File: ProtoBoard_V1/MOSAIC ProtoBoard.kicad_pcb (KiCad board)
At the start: 2 copper layers, 89.5 x 90 mm, 10 parts, among them J7 Qwiic Adapter, J8 Qwiic Adapter, J9 Qwiic Adapter

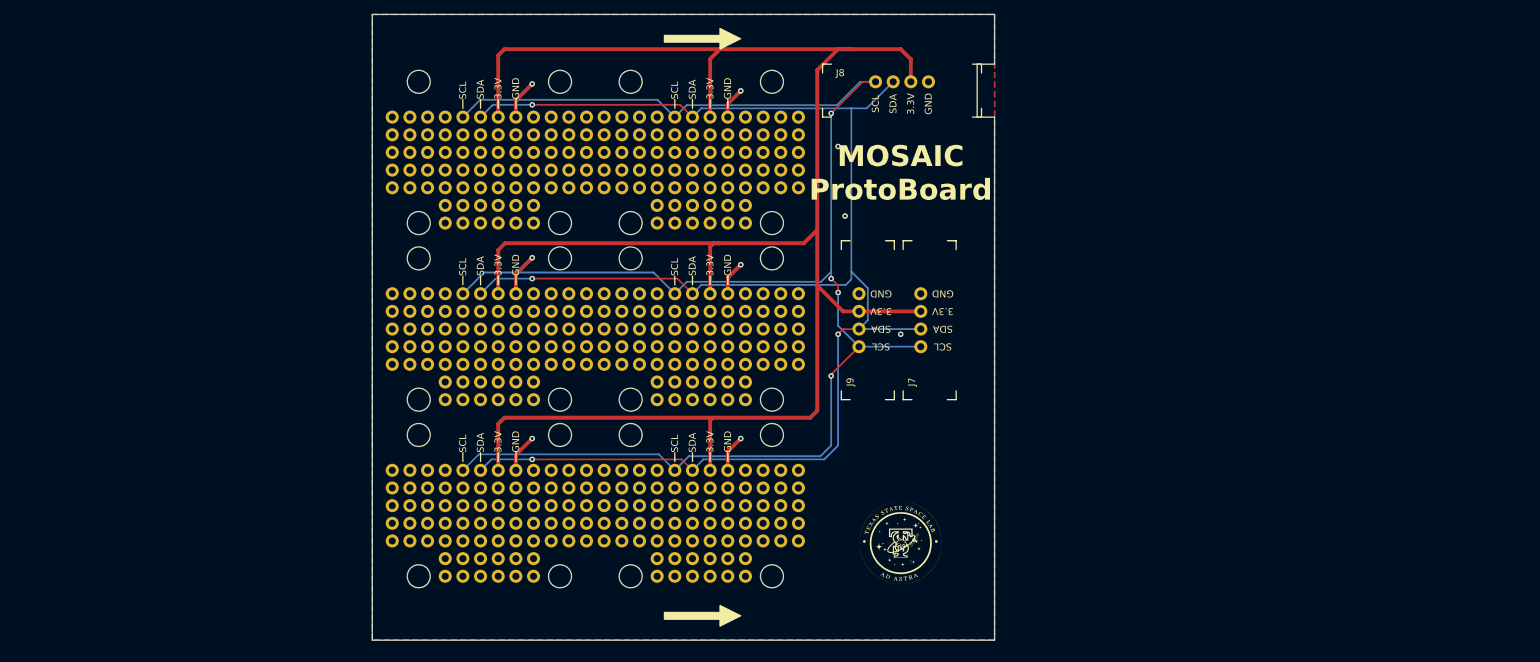
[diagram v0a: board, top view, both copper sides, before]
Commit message: Created new edge cut
Created new edge cut for the board based on new standard size
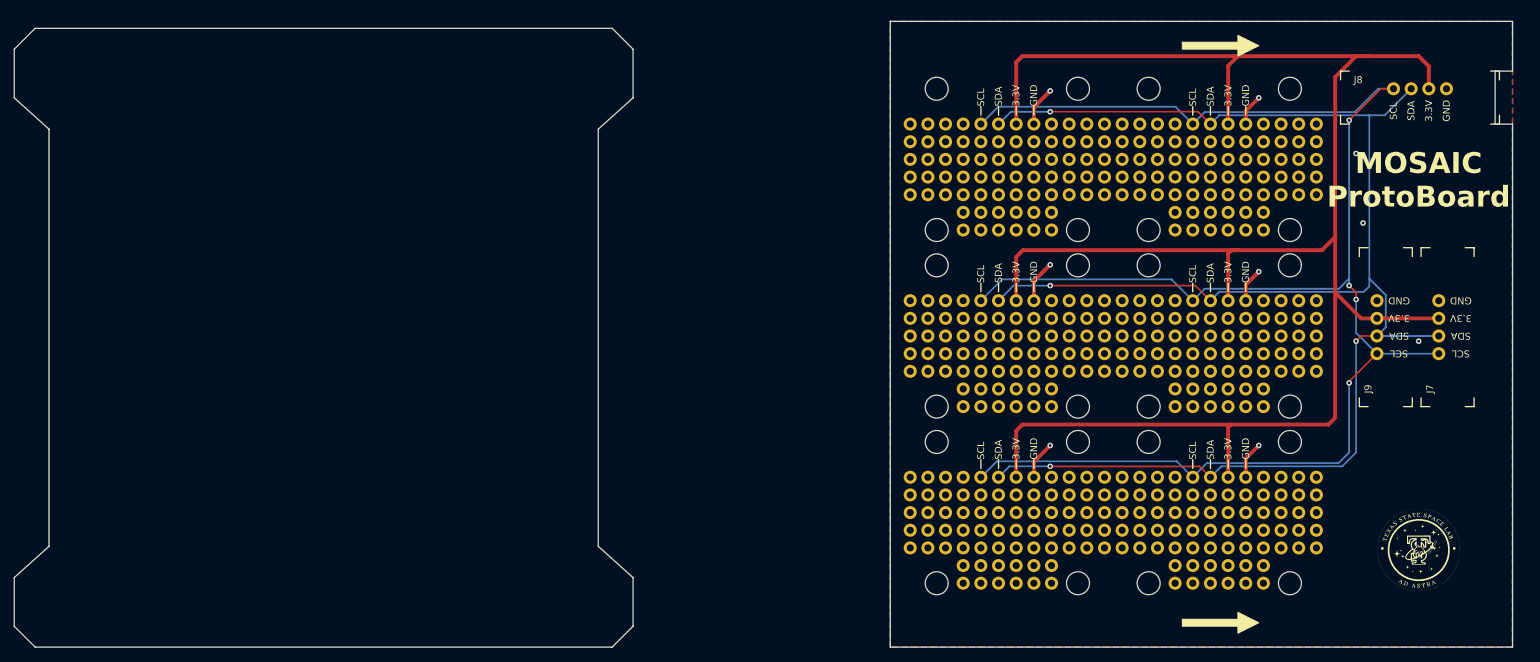
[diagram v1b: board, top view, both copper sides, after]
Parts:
- moved G*** 74.5 mm to (250.4, 126.8)
- moved J1 74.5 mm to (181.2, 60.7)
- moved J2 74.5 mm to (211.7, 86.1)
- moved J3 74.5 mm to (181.2, 86.1)
- moved J4 74.5 mm to (211.7, 111.5)
- moved J5 74.5 mm to (181.2, 111.5)
- moved J6 74.5 mm to (211.7, 60.7)
- moved J7 74.5 mm to (250.8, 106.4)
- moved J8 74.5 mm to (239.3, 58.1)
- moved J9 74.5 mm to (242.0, 106.4)
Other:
- board size 89.5 x 90 mm -> 215.5 x 90 mm

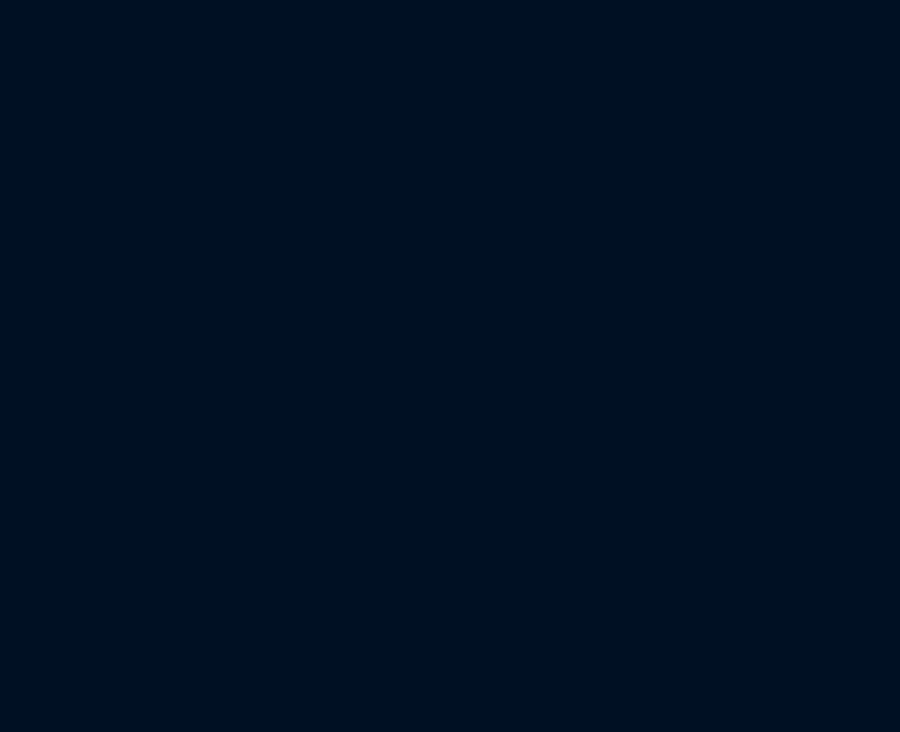
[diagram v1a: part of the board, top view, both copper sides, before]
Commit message: Added circle mount holes to PCB
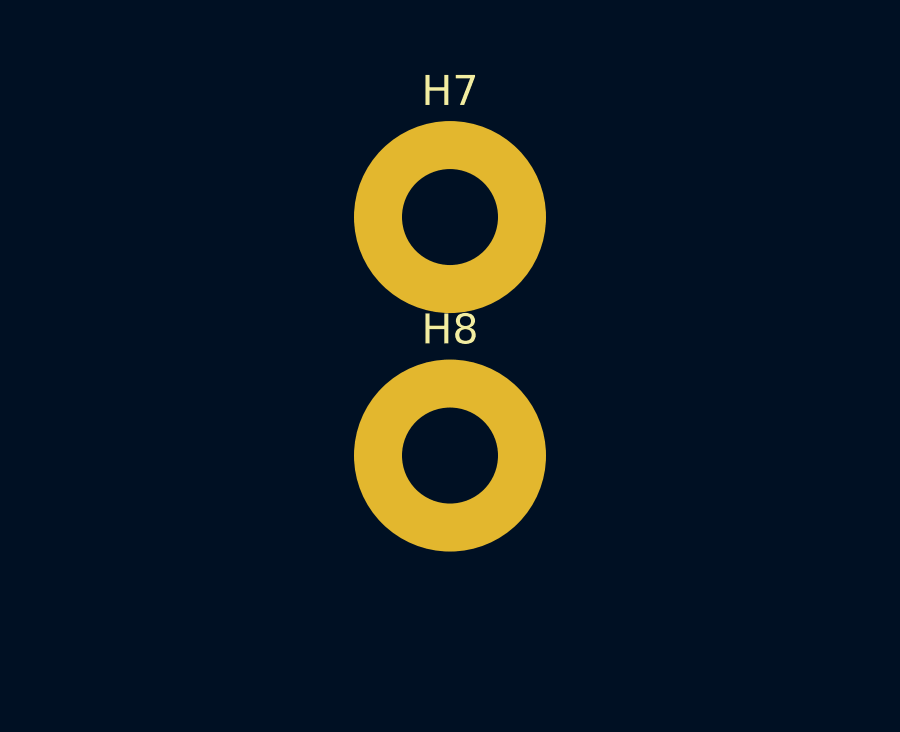
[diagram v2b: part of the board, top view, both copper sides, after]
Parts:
- added H7: MountingHole_Pad, MountingHole:MountingHole_3.2mm_M3_Pad, F.Cu at (91.1, -28.6)
- added H8: MountingHole_Pad, MountingHole:MountingHole_3.2mm_M3_Pad, F.Cu at (91.1, -20.6)
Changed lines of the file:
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@@
 			)
 		)
+		(sheetname "/")
 		(sheetfile "MOSAIC ProtoBoard.kicad_sch")
 		(attr smd)
@@
 			)
 		)
+		(sheetname "/")
 		(sheetfile "MOSAIC ProtoBoard.kicad_sch")
 		(attr smd)
@@
 			)
 		)
+		(sheetname "/")
 		(sheetfile "MOSAIC ProtoBoard.kicad_sch")
 		(attr smd)
@@
 			)
 		)
+		(sheetname "/")
 		(sheetfile "MOSAIC ProtoBoard.kicad_sch")
 		(attr smd)
@@
 			)
 		)
+		(sheetname "/")
 		(sheetfile "MOSAIC ProtoBoard.kicad_sch")
 		(attr smd)
@@
 			)
 		)
+		(sheetname "/")
 		(sheetfile "MOSAIC ProtoBoard.kicad_sch")
 		(attr smd)
@@
 		(embedded_fonts no)
 	)
+	(footprint "MountingHole:MountingHole_3.2mm_M3_Pad"
+		(layer "F.Cu")
+		(at 91.1 -20.6)
+		(descr "Mounting Hole 3.2mm, M3")
+		(tags "mounting hole 3.2mm m3")
+		(property "Reference" "H8"
+			(at 0 -4.2 0)
+			(layer "F.SilkS")
+			(effects
+				(font
+					(size 1 1)
+					(thickness 0.15)
+				)
+			)
+		)
+		(property "Value" "MountingHole_Pad"
+			(at 0 4.2 0)
+			(layer "F.Fab")
+			(effects
+				(font
+					(size 1 1)
+					(thickness 0.15)
+				)
+			)
+		)
+		(property "Datasheet" ""
+			(at 0 0 0)
+			(unlocked yes)
+			(layer "F.Fab")
+			(hide yes)
+			(effects
+				(font
+					(size 1.27 1.27)
+					(thickness 0.15)
+				)
+			)
+		)
+		(property "Description" "Mounting Hole with connection"
+			(at 0 0 0)
+			(unlocked yes)
+			(layer "F.Fab")
+			(hide yes)
+			(effects
+				(font
+					(size 1.27 1.27)
+					(thickness 0.15)
+				)
+			)
+		)
+		(property ki_fp_filters "MountingHole*Pad*")
+		(sheetname "/")
+		(sheetfile "MOSAIC ProtoBoard.kicad_sch")
+		(attr exclude_from_pos_files exclude_from_bom)
+		(fp_circle
+			(center 0 0)
+			(end 3.2 0)
+			(stroke
+				(width 0.15)
+				(type solid)
+			)
+			(fill no)
+			(layer "Cmts.User")
+		)
+		(fp_circle
+			(center 0 0)
+			(end 3.45 0)
+			(stroke
+				(width 0.05)
+				(type solid)
+			)
+			(fill no)
+			(layer "F.CrtYd")
+		)
+		(fp_text user "${REFERENCE}"
+			(at 0 0 0)
+			(layer "F.Fab")
+			(effects
+				(font
+					(size 1 1)
+					(thickness 0.15)
+				)
+			)
+		)
+		(pad "1" thru_hole circle
+			(at 0 0)
+			(size 6.4 6.4)
+			(drill 3.2)
+			(layers "*.Cu" "*.Mask")
+			(remove_unused_layers no)
+			(net 2 "GND")
+			(pinfunction "1")
+			(pintype "input")
+		)
+		(embedded_fonts no)
+	)
 	(footprint "MOSAIC_ProtoBoard:QWIIC_2_Adapter"
 		(layer "F.Cu")
@@
 			)
 		)
+		(sheetname "/")
 		(sheetfile "MOSAIC ProtoBoard.kicad_sch")
 		(attr smd)
@@
 		(embedded_fonts no)
 	)
+	(footprint "MountingHole:MountingHole_3.2mm_M3_Pad"
+		(layer "F.Cu")
+		(at 91.1 -28.55)
+		(descr "Mounting Hole 3.2mm, M3")
+		(tags "mounting hole 3.2mm m3")
+		(property "Reference" "H7"
+			(at 0 -4.2 0)
+			(layer "F.SilkS")
+			(effects
+				(font
+					(size 1 1)
+					(thickness 0.15)
+				)
+			)
+		)
+		(property "Value" "MountingHole_Pad"
+			(at 0 4.2 0)
+			(layer "F.Fab")
+			(effects
+				(font
+					(size 1 1)
+					(thickness 0.15)
+				)
+			)
+		)
+		(property "Datasheet" ""
+			(at 0 0 0)
+			(unlocked yes)
+			(layer "F.Fab")
+			(hide yes)
+			(effects
+				(font
+					(size 1.27 1.27)
+					(thickness 0.15)
+				)
+			)
+		)
+		(property "Description" "Mounting Hole with connection"
+			(at 0 0 0)
+			(unlocked yes)
+			(layer "F.Fab")
+			(hide yes)
+			(effects
+				(font
+					(size 1.27 1.27)
+					(thickness 0.15)
+				)
+			)
+		)
+		(property ki_fp_filters "MountingHole*Pad*")
+		(sheetname "/")
+		(sheetfile "MOSAIC ProtoBoard.kicad_sch")
+		(attr exclude_from_pos_files exclude_from_bom)
+		(fp_circle
+			(center 0 0)
+			(end 3.2 0)
+			(stroke
+				(width 0.15)
+				(type solid)
+			)
+			(fill no)
+			(layer "Cmts.User")
+		)
+		(fp_circle
+			(center 0 0)
+			(end 3.45 0)
+			(stroke
+				(width 0.05)
+				(type solid)
+			)
+			(fill no)
+			(layer "F.CrtYd")
+		)
+		(fp_text user "${REFERENCE}"
+			(at 0 0 0)
+			(layer "F.Fab")
+			(effects
+				(font
+					(size 1 1)
+					(thickness 0.15)
+				)
+			)
+		)
+		(pad "1" thru_hole circle
+			(at 0 0)
+			(size 6.4 6.4)
+			(drill 3.2)
+			(layers "*.Cu" "*.Mask")
+			(remove_unused_layers no)
+			(net 2 "GND")
+			(pinfunction "1")
+			(pintype "input")
+		)
+		(embedded_fonts no)
+	)
 	(footprint "MOSAIC_ProtoBoard:QWIIC_Sensor_CONN"
 		(layer "F.Cu")
@@
 			)
 		)
+		(sheetname "/")
 		(sheetfile "MOSAIC ProtoBoard.kicad_sch")
 		(attr smd)
@@
 			)
 		)
+		(sheetname "/")
 		(sheetfile "MOSAIC ProtoBoard.kicad_sch")
 		(attr smd)

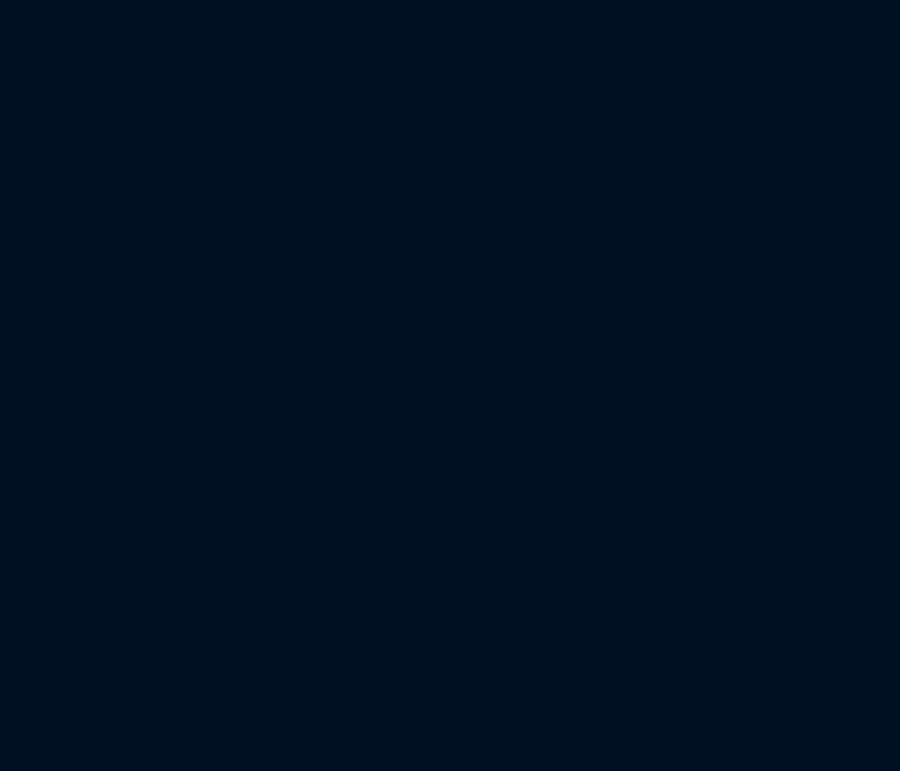
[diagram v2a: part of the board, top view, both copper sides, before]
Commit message: Add mounts to schem and board
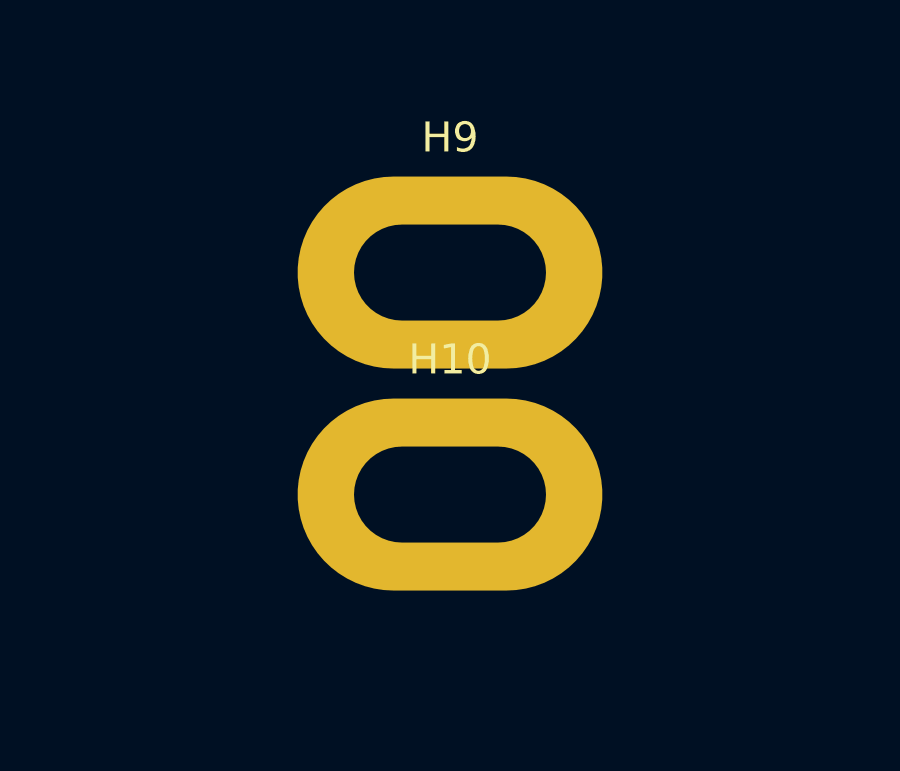
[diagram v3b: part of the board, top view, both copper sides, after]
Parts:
- added H10: MountingHole_Pad, protoboard_footprints_V1.0:MountingHole_3.2mm_Pad_Oval, F.Cu at (123.1, -19.3)
- added H9: MountingHole_Pad, protoboard_footprints_V1.0:MountingHole_3.2mm_Pad_Oval, F.Cu at (123.1, -26.7)
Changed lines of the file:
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@@
 		(embedded_fonts no)
 	)
+	(footprint "protoboard_footprints_V1.0:MountingHole_3.2mm_Pad_Oval"
+		(layer "F.Cu")
+		(at 123.1 -19.3)
+		(property "Reference" "H10"
+			(at 0 -4.5 0)
+			(unlocked yes)
+			(layer "F.SilkS")
+			(effects
+				(font
+					(size 1 1)
+					(thickness 0.1)
+				)
+			)
+		)
+		(property "Value" "MountingHole_Pad"
+			(at 0 5.5 0)
+			(unlocked yes)
+			(layer "F.Fab")
+			(effects
+				(font
+					(size 1 1)
+					(thickness 0.15)
+				)
+			)
+		)
+		(property "Datasheet" ""
+			(at 0 0 0)
+			(unlocked yes)
+			(layer "F.Fab")
+			(hide yes)
+			(effects
+				(font
+					(size 1 1)
+					(thickness 0.15)
+				)
+			)
+		)
+		(property "Description" "Mounting Hole with connection"
+			(at 0 0 0)
+			(unlocked yes)
+			(layer "F.Fab")
+			(hide yes)
+			(effects
+				(font
+					(size 1 1)
+					(thickness 0.15)
+				)
+			)
+		)
+		(property ki_fp_filters "MountingHole*Pad*")
+		(sheetname "/")
+		(sheetfile "MOSAIC ProtoBoard.kicad_sch")
+		(attr exclude_from_pos_files exclude_from_bom)
+		(fp_text user "${REFERENCE}"
+			(at 0 8 0)
+			(unlocked yes)
+			(layer "F.Fab")
+			(effects
+				(font
+					(size 1 1)
+					(thickness 0.15)
+				)
+			)
+		)
+		(pad "1" thru_hole oval
+			(at 0 0)
+			(size 10.16 6.400013)
+			(drill oval 6.400013 3.199994)
+			(layers "*.Cu" "*.Mask")
+			(remove_unused_layers no)
+			(net 2 "GND")
+			(pinfunction "1")
+			(pintype "input")
+			(thermal_bridge_angle 45)
+		)
+		(embedded_fonts no)
+	)
 	(footprint "protoboard_footprints_V1.0:SL_Logo"
 		(layer "F.Cu")
@@
 		)
 		(embedded_fonts no)
+	)
+	(footprint "protoboard_footprints_V1.0:MountingHole_3.2mm_Pad_Oval"
+		(layer "F.Cu")
+		(at 123.1 -26.700014)
+		(property "Reference" "H9"
+			(at 0 -4.5 0)
+			(unlocked yes)
+			(layer "F.SilkS")
+			(effects
+				(font
+					(size 1 1)
+					(thickness 0.1)
+				)
+			)
+		)
+		(property "Value" "MountingHole_Pad"
+			(at 0 5.5 0)
+			(unlocked yes)
+			(layer "F.Fab")
+			(effects
+				(font
+					(size 1 1)
+					(thickness 0.15)
+				)
+			)
+		)
+		(property "Datasheet" ""
+			(at 0 0 0)
+			(unlocked yes)
+			(layer "F.Fab")
+			(hide yes)
+			(effects
+				(font
+					(size 1 1)
+					(thickness 0.15)
+				)
+			)
+		)
+		(property "Description" "Mounting Hole with connection"
+			(at 0 0 0)
+			(unlocked yes)
+			(layer "F.Fab")
+			(hide yes)
+			(effects
+				(font
+					(size 1 1)
+					(thickness 0.15)
+				)
+			)
+		)
+		(property ki_fp_filters "MountingHole*Pad*")
+		(sheetname "/")
+		(sheetfile "MOSAIC ProtoBoard.kicad_sch")
+		(attr exclude_from_pos_files exclude_from_bom)
+		(fp_text user "${REFERENCE}"
+			(at 0 8 0)
+			(unlocked yes)
+			(layer "F.Fab")
+			(effects
+				(font
+					(size 1 1)
+					(thickness 0.15)
+				)
+			)
+		)
+		(pad "1" thru_hole oval
+			(at 0 0)
+			(size 10.16 6.400013)
+			(drill oval 6.400013 3.199994)
+			(layers "*.Cu" "*.Mask")
+			(remove_unused_layers no)
+			(net 2 "GND")
+			(pinfunction "1")
+			(pintype "input")
+			(thermal_bridge_angle 45)
+		)
+		(embedded_fonts no)

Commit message: Positioning and routing
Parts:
- moved J9 181.4 mm to (62.0, 83.3), turned to -90 degrees
- moved J8 174.4 mm to (81.8, 133.0)
- moved H7 167.3 mm to (130.5, 134.0)
- moved H8 158.6 mm to (55.5, 134.0)
- moved J7 126.9 mm to (124.0, 106.0)
- moved J1 113.7 mm to (67.5, 59.2)
- moved J3 113.7 mm to (67.5, 84.6)
- moved J5 113.7 mm to (67.5, 110.0)
- moved J2 113.7 mm to (98.0, 84.6)
- moved J4 113.7 mm to (98.0, 110.0)
- moved J6 113.7 mm to (98.0, 59.2)
- moved H9 109.2 mm to (55.5, 59.0), turned to 90 degrees
- moved H10 78.6 mm to (130.5, 59.0), turned to 90 degrees
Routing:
- net /SDA: track 235.7 -> 363.0 mm, vias 4 -> 0
- net /SCL: track 244.9 -> 368.0 mm, vias 4 -> 8
- net VIN: track 277.3 -> 325.2 mm
- net GND: track 32.3 -> 0.00 mm, vias 9 -> 2
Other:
- board size 215.5 x 90 mm -> 89 x 89 mm

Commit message: Finished placement and routing
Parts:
- removed the G*** at (250.4, 126.8)
- added G***: LOGO, LOGO, F.Cu at (172.0, 62.5)
- added G***: LOGO, LOGO, F.Cu at (219.0, 132.0)
- added G***: LOGO, LOGO, F.Cu at (194.0, 181.0)
- added LOGO2: OSHW-LOGOL, protoboard_footprints_V1.0:OSHW-LOGO-L, F.Cu at (227.5, 133.0)
- J1, J2, J3, J4, J5, J6: footprint MOSAIC_ProtoBoard:QWIIC_Sensor_CONN -> protoboard_footprints_V1.0:QWIIC_Sensor_CONN
- J7, J8, J9: footprint MOSAIC_ProtoBoard:QWIIC_2_Adapter -> protoboard_footprints_V1.0:QWIIC_2_Adapter
- moved H9 182.5 mm to (238.0, 60.0), turned to 0 degrees
- moved J1 170.8 mm to (237.8, 72.0), turned to -90 degrees
- moved J9 152.7 mm to (213.7, 66.5), turned to 180 degrees
- moved J6 146.4 mm to (237.8, 102.5), turned to -90 degrees
- moved J3 145.5 mm to (212.4, 72.0), turned to -90 degrees
- moved H10 131.7 mm to (238.0, 135.0), turned to 0 degrees
- moved H8 130.5 mm to (163.0, 60.0), turned to -90 degrees
- moved J5 125.4 mm to (187.0, 72.0), turned to -90 degrees
- moved J2 115.8 mm to (212.4, 102.5), turned to -90 degrees
- moved J8 94.6 mm to (164.0, 86.3), turned to -90 degrees
- moved J4 89.4 mm to (187.0, 102.5), turned to -90 degrees
- moved J7 70.7 mm to (191.0, 128.5), turned to 0 degrees
- moved H7 32.5 mm to (163.0, 135.0), turned to -90 degrees
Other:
- outline, holes or cut-outs redrawn
- board text added: "MOSAIC"
- board text added: "ProtoBoard"
- board text added: "V1.0"
- board text removed: "MOSAIC ProtoBoard"
